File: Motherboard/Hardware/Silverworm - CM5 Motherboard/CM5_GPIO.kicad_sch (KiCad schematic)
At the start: 28 parts, among them J14 JST_SHBM04B-SRSS-TB, J2 Conn_02x07_Odd_Even, J3 Conn_01x03, J7 Micro_SD_Card_Det, J8 THD-20-R, J9 THD-02-R, SW1 Right angle Tact button, U1 TPD4EUSB30, U18 RT9742GGJ5, U2 TPD4EUSB30, U3 MagJack-A70-112-331N126

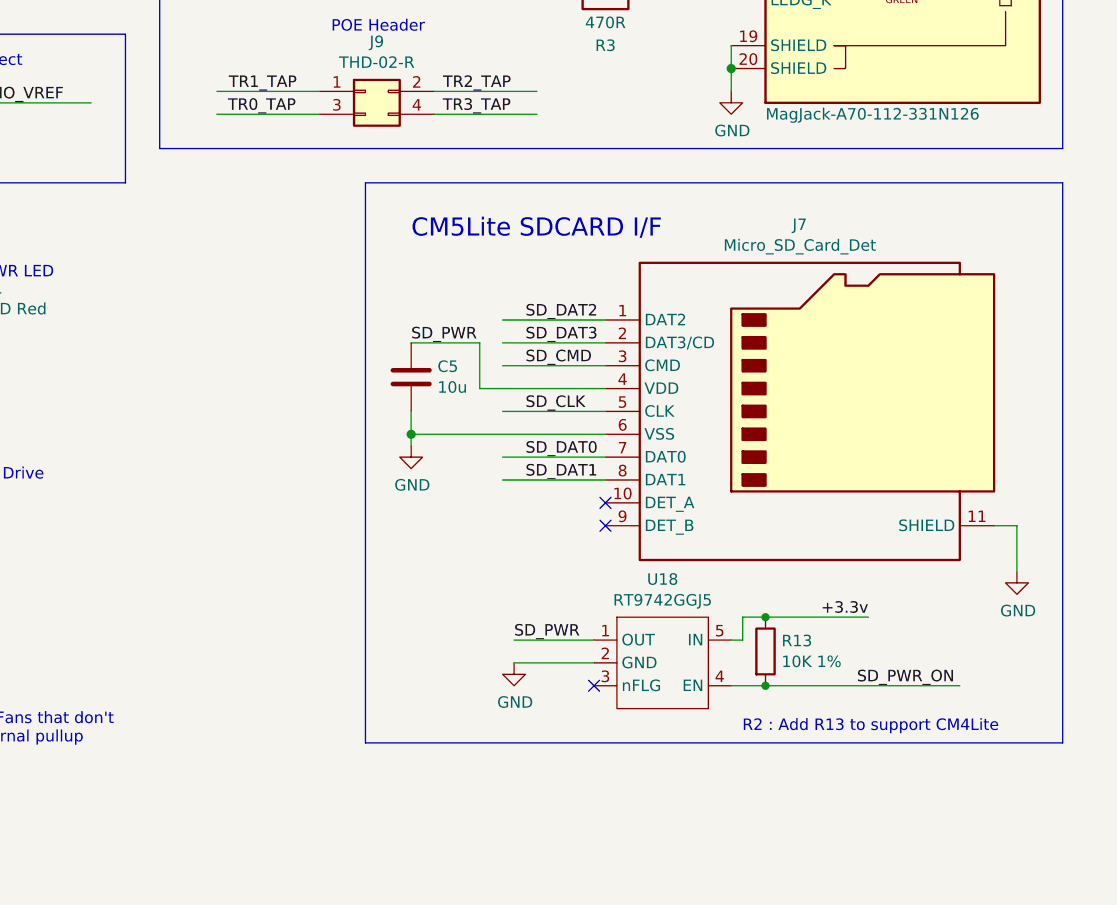
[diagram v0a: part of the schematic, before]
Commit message: Added footprints and board connectors
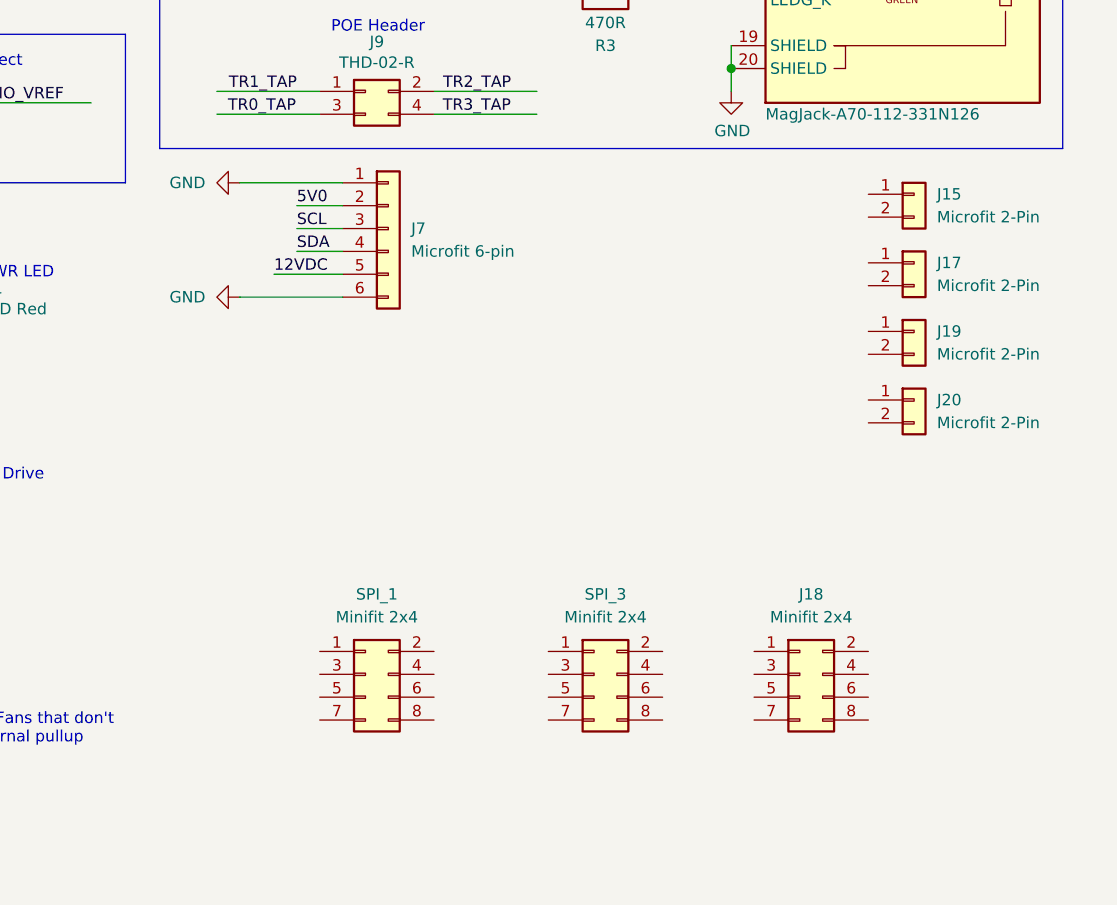
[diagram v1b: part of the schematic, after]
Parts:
- removed C5: 10u, Capacitor_SMD:C_0805_2012Metric, symbol Device:C
- removed J7: Micro_SD_Card_Det, CM5IO:SDCARD_MOLEX_503398-1892, symbol Connector:Micro_SD_Card_Det2
- removed R13: 10K 1%, Resistor_SMD:R_0402_1005Metric, symbol Device:R
- removed U18: RT9742GGJ5, Package_TO_SOT_SMD:SOT-23-5, symbol CM5IO:RT9742GGJ5
- added J15, J17, J19, J20: Microfit 2-Pin, symbol Connector_Generic:Conn_01x02
- added J18, SPI_1, SPI_3: Minifit 2x4, Connector_Molex:Molex_Mini-Fit_Jr_5569-08A2_2x04_P4.20mm_Horizontal, symbol Connector_Generic:Conn_02x04_Odd_Even
- added J7: Microfit 6-pin, Connector_Molex:Molex_Micro-Fit_3.0_43045-0621_2x03-1MP_P3.00mm_Horizontal, symbol Connector_Generic:Conn_01x06
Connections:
- net GND: now also J7.1 (Pin_1), J7.6 (Pin_6)
- new net 12VDC: J7.5 (Pin_5)
- new net 5V0: J7.2 (Pin_2)
- new net SCL: J7.3 (Pin_3)
- new net SDA: J7.4 (Pin_4)
- no-connect marks 9 -> 6
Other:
- note removed: "CM5Lite SDCARD I/F"
- note removed: "R2 : Add R13 to support CM4Lite"

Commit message: Layout and IO edits
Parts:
- removed J18, SPI_3: Minifit 2x4, Connector_Molex:Molex_Mini-Fit_Jr_5569-08A2_2x04_P4.20mm_Horizontal, symbol Connector_Generic:Conn_02x04_Odd_Even
- added J18: JST-SM, symbol Connector_Generic:Conn_01x03
- added R13: 470R, symbol Device:R
- added R21, R22, R23, R24: 10K, symbol Device:R
- added SPI_3, SPI_5: Minifit 2x4, Connector_Molex:Molex_Mini-Fit_Jr_5569-08A2_2x04_P4.20mm_Horizontal, symbol Connector_Generic:Conn_02x04_Counter_Clockwise
- SPI_1: symbol Connector_Generic:Conn_02x04_Odd_Even -> Connector_Generic:Conn_02x04_Counter_Clockwise
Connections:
- net +3.3v: now also R21.1, R22.1, R23.1, R24.1
- net 12VDC: now also SPI_1.6 (Pin_6), SPI_3.6 (Pin_6), SPI_5.6 (Pin_6)
- net 5V0: now also SPI_1.7 (Pin_7), J18.3 (Pin_3), SPI_3.7 (Pin_7), SPI_5.7 (Pin_7)
- net GND: now also J15.2 (Pin_2), J17.2 (Pin_2), J19.2 (Pin_2), J20.2 (Pin_2), SPI_1.5 (Pin_5), SPI_1.8 (Pin_8), J18.1 (Pin_1), SPI_3.5 (Pin_5), SPI_3.8 (Pin_8), SPI_5.5 (Pin_5), SPI_5.8 (Pin_8)
- net GPIO10: no longer Module1.44 (GPIO10)
- net GPIO14: no longer Module1.55 (GPIO14)
- net GPIO17: no longer Module1.50 (GPIO17)
- net GPIO18: no longer Module1.49 (GPIO18)
- net GPIO19: no longer Module1.26 (GPIO19)
- net GPIO20: no longer Module1.27 (GPIO20)
- net GPIO21: no longer Module1.25 (GPIO21)
- net GPIO22: no longer Module1.46 (GPIO22)
- net GPIO27: no longer Module1.48 (GPIO27)
- net GPIO4: no longer Module1.54 (GPIO4)
- net GPIO5: no longer Module1.34 (GPIO5)
- net GPIO6: no longer Module1.30 (GPIO6)
- net GPIO7: no longer Module1.37 (GPIO7)
- net LK_3: now reaches J19.1 (Pin_1)
- net LK_3: now also Module1.48 (GPIO27), R23.2
- net MOSI_1: now reaches SPI_1.1 (Pin_1)
- net MOSI_1: now also Module1.27 (GPIO20)
- net MISO_1: now reaches SPI_1.2 (Pin_2)
- net MISO_1: now also Module1.26 (GPIO19)
- net SCLK_1: now reaches SPI_1.3 (Pin_3)
- net SCLK_1: now also Module1.25 (GPIO21)
- net CSn_1: now reaches SPI_1.4 (Pin_4)
- net CSn_1: now also Module1.49 (GPIO18)
- net LK_2: now reaches J17.1 (Pin_1)
- net LK_2: now also Module1.46 (GPIO22), R22.2
- net LK_4: now reaches J20.1 (Pin_1)
- net LK_4: now also Module1.50 (GPIO17), R24.2
- net LK_1: now reaches J15.1 (Pin_1)
- net LK_1: now also Module1.44 (GPIO10), R21.2
- new net: J18.2 (Pin_2), R13.2
- new net CSn_3: Module1.54 (GPIO4), SPI_3.4 (Pin_4)
- new net LED_DATA: Module1.55 (GPIO14), R13.1
- new net MISO_3: Module1.34 (GPIO5), SPI_3.2 (Pin_2)
- new net MOSI_3: Module1.30 (GPIO6), SPI_3.1 (Pin_1)
- new net SCLK_3: Module1.37 (GPIO7), SPI_3.3 (Pin_3)
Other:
- note added: "Door Lock Inputs"
- note added: "RGB LED Connection"
- note added: "SPI Interfaces"
- note added: "UI Panel Connection"
- title: Compute Module 5 IO Board - Top Level -> Silverworm CM5 Motherboard - GPIO
- moved on the sheet: D1, J14, J15, J17, J19, J20, J7, R10, R11, SPI_1, SW1, TP2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

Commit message: PCB changes (many)
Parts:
- removed SPI_5: Minifit 2x4, Connector_Molex:Molex_Mini-Fit_Jr_5569-08A2_2x04_P4.20mm_Horizontal, symbol Connector_Generic:Conn_02x04_Counter_Clockwise
- J12: renamed from J18; value JST-SM -> Microfit 3-pin; footprint (none) -> Connector_Molex:Molex_Micro-Fit_3.0_43650-0315_1x03_P3.00mm_Vertical
- J15: footprint (none) -> Connector_Molex:Molex_Micro-Fit_3.0_43650-0215_1x02_P3.00mm_Vertical
- J16: renamed from J17; footprint (none) -> Connector_Molex:Molex_Micro-Fit_3.0_43650-0215_1x02_P3.00mm_Vertical
- J17: renamed from J19; footprint (none) -> Connector_Molex:Molex_Micro-Fit_3.0_43650-0215_1x02_P3.00mm_Vertical
- J18: renamed from J20; footprint (none) -> Connector_Molex:Molex_Micro-Fit_3.0_43650-0215_1x02_P3.00mm_Vertical
- R10: renamed from R13; footprint (none) -> Resistor_SMD:R_0402_1005Metric
- R16: renamed from R21; footprint (none) -> Resistor_SMD:R_0402_1005Metric
- R17: renamed from R22; footprint (none) -> Resistor_SMD:R_0402_1005Metric
- R18: renamed from R23; footprint (none) -> Resistor_SMD:R_0402_1005Metric
- R19: renamed from R24; footprint (none) -> Resistor_SMD:R_0402_1005Metric
- renumbered C1 to C9, D2 to D1, D1 to D2, J3 to J10, J8 to J11, J9 to J13, J7 to J14, J2 to J8, J14 to J9, R5 to R11, R4 to R12, R10 to R13, R2 to R14, R3 to R15, R11 to R8, R1 to R9, SPI_3 to SPI_2, TP2 to TP1, TP4 to TP2, TP5 to TP4, U1 to U3, U2 to U4, U3 to U5
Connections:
- net 5V0 is gone; now on net +5V: J12.3 (Pin_3), J14.2 (Pin_2), SPI_1.7 (Pin_7), SPI_2.7 (Pin_7)
- net +5v renamed +5V
- net 12VDC renamed +24V
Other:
- moved on the sheet: J14, SPI_2

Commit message: motherboard layout
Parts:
- J15, J16, J17, J18: footprint Connector_Molex:Molex_Micro-Fit_3.0_43650-0215_1x02_P3.00mm_Vertical -> Connector_Molex:Molex_Micro-Fit_3.0_43045-0221_2x01-1MP_P3.00mm_Horizontal
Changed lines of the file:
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@@
 			)
 		)
-		(property "Footprint" "Connector_Molex:Molex_Micro-Fit_3.0_43650-0215_1x02_P3.00mm_Vertical"
+		(property "Footprint" "Connector_Molex:Molex_Micro-Fit_3.0_43045-0221_2x01-1MP_P3.00mm_Horizontal"
 			(at 264.16 135.89 0)
 			(effects
@@
 		(exclude_from_sim no)
 		(in_bom no)
-		(on_board yes)
+		(on_board no)
 		(dnp yes)
 		(property "Reference" "TP1"
@@
 			)
 		)
-		(property "Footprint" "Connector_Molex:Molex_Micro-Fit_3.0_43650-0215_1x02_P3.00mm_Vertical"
+		(property "Footprint" "Connector_Molex:Molex_Micro-Fit_3.0_43045-0221_2x01-1MP_P3.00mm_Horizontal"
 			(at 264.16 124.46 0)
 			(effects
@@
 			)
 		)
-		(property "Footprint" "Connector_Molex:Molex_Micro-Fit_3.0_43650-0215_1x02_P3.00mm_Vertical"
+		(property "Footprint" "Connector_Molex:Molex_Micro-Fit_3.0_43045-0221_2x01-1MP_P3.00mm_Horizontal"
 			(at 264.16 146.05 0)
 			(effects
@@
 			)
 		)
-		(property "Footprint" "Connector_Molex:Molex_Micro-Fit_3.0_43650-0215_1x02_P3.00mm_Vertical"
+		(property "Footprint" "Connector_Molex:Molex_Micro-Fit_3.0_43045-0221_2x01-1MP_P3.00mm_Horizontal"
 			(at 264.16 114.3 0)
 			(effects

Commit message: finalised motherboard
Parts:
- added JP1: Jumper_2_Open, Jumper:SolderJumper-2_P1.3mm_Open_RoundedPad1.0x1.5mm, symbol Jumper:Jumper_2_Open
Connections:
- net SCL is gone; now on net GPIO11: J14.3 (Pin_3)
- net SDA is gone; now on net GPIO10: J14.4 (Pin_4)
- net +24V: now also JP1.1 (A); no longer J14.5 (Pin_5)
- net GPIO10: now also Module1.44 (GPIO10)
- net GPIO9: now also J15.1 (Pin_1), R16.2
- removed net LK_1: J15.1 (Pin_1), Module1.44 (GPIO10), R16.2
- new net: J14.5 (Pin_5), JP1.2 (B)
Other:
- moved on the sheet: J12, R10
